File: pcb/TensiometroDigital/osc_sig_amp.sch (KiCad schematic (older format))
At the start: 9 parts

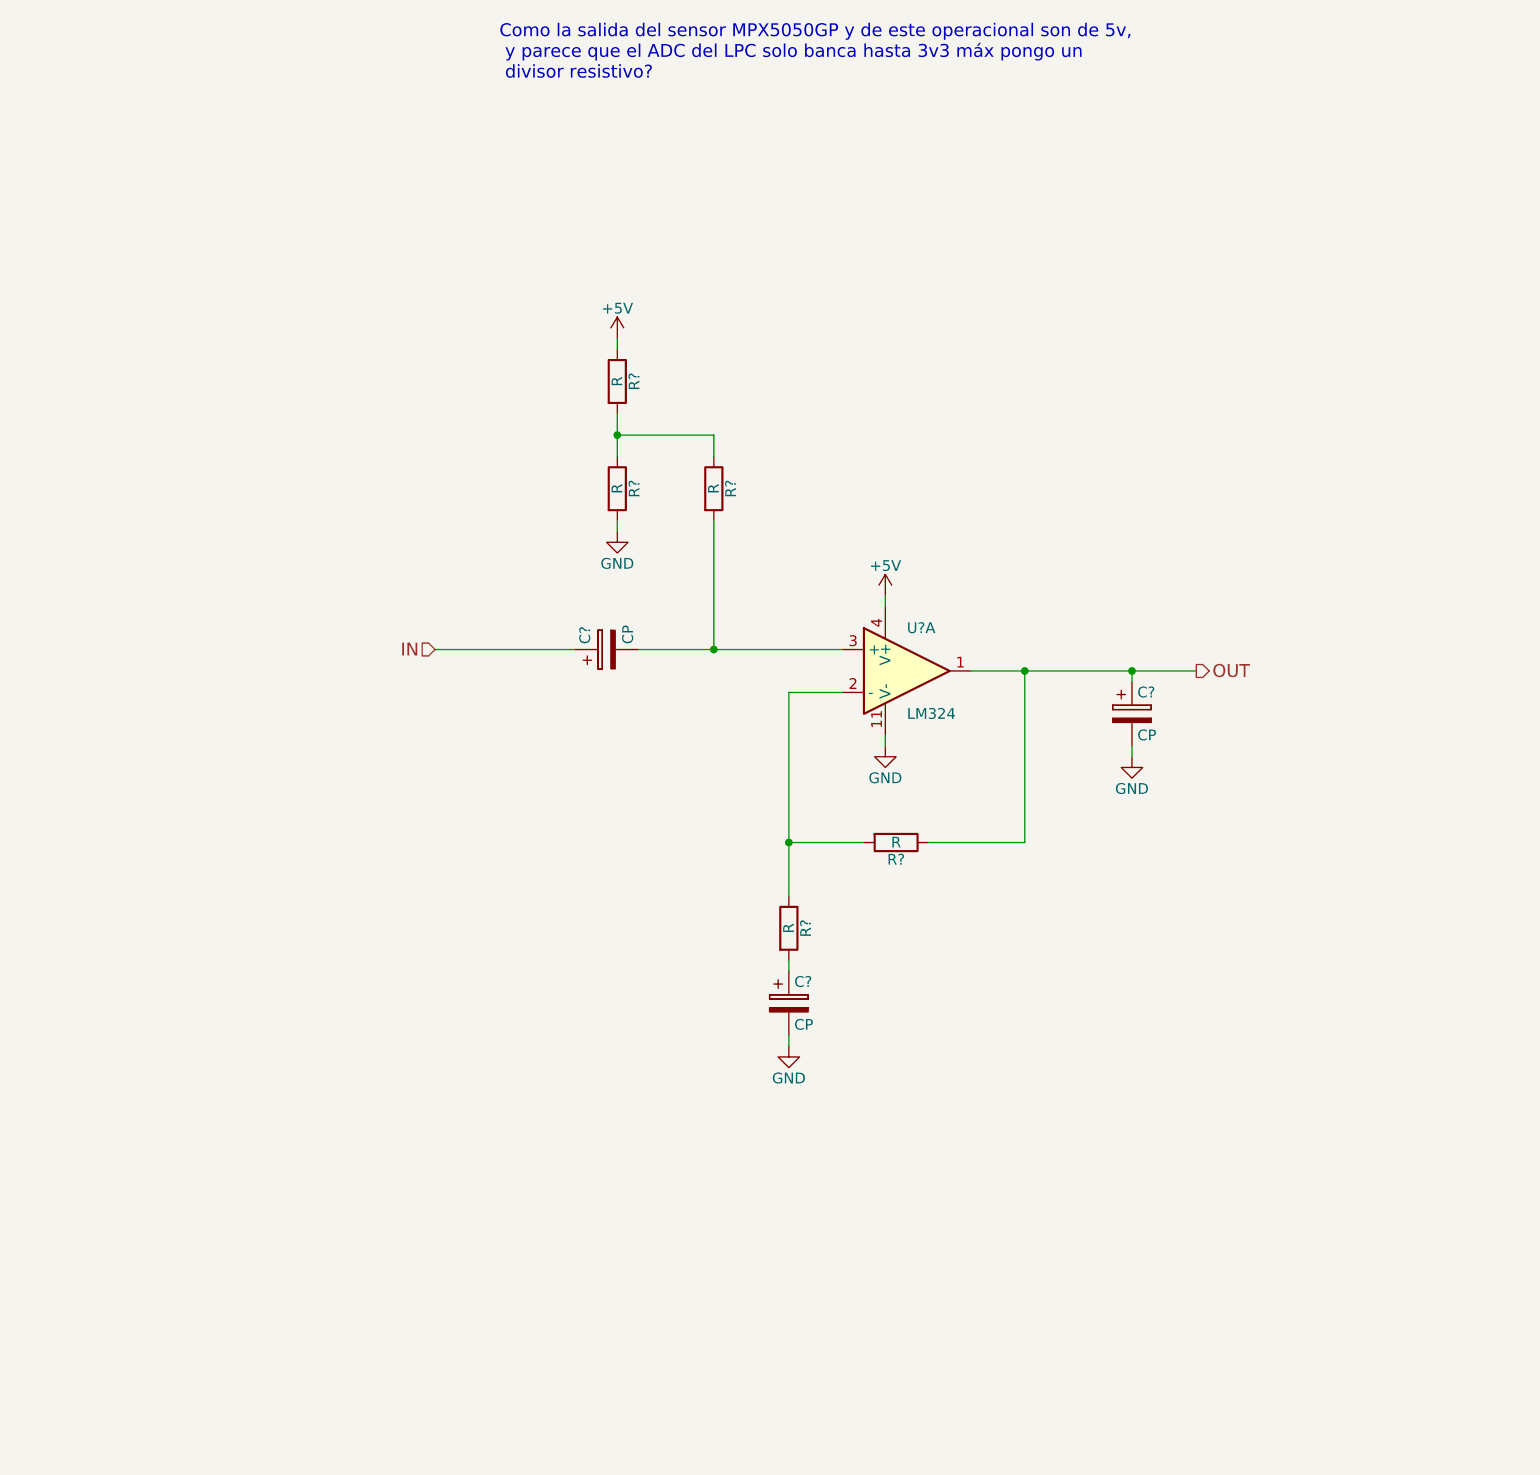
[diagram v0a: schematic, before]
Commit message: Finalizado: SCH, PCB, GABINETE, DRAWINGS. FALTA: GERBERS, BOM e Informe
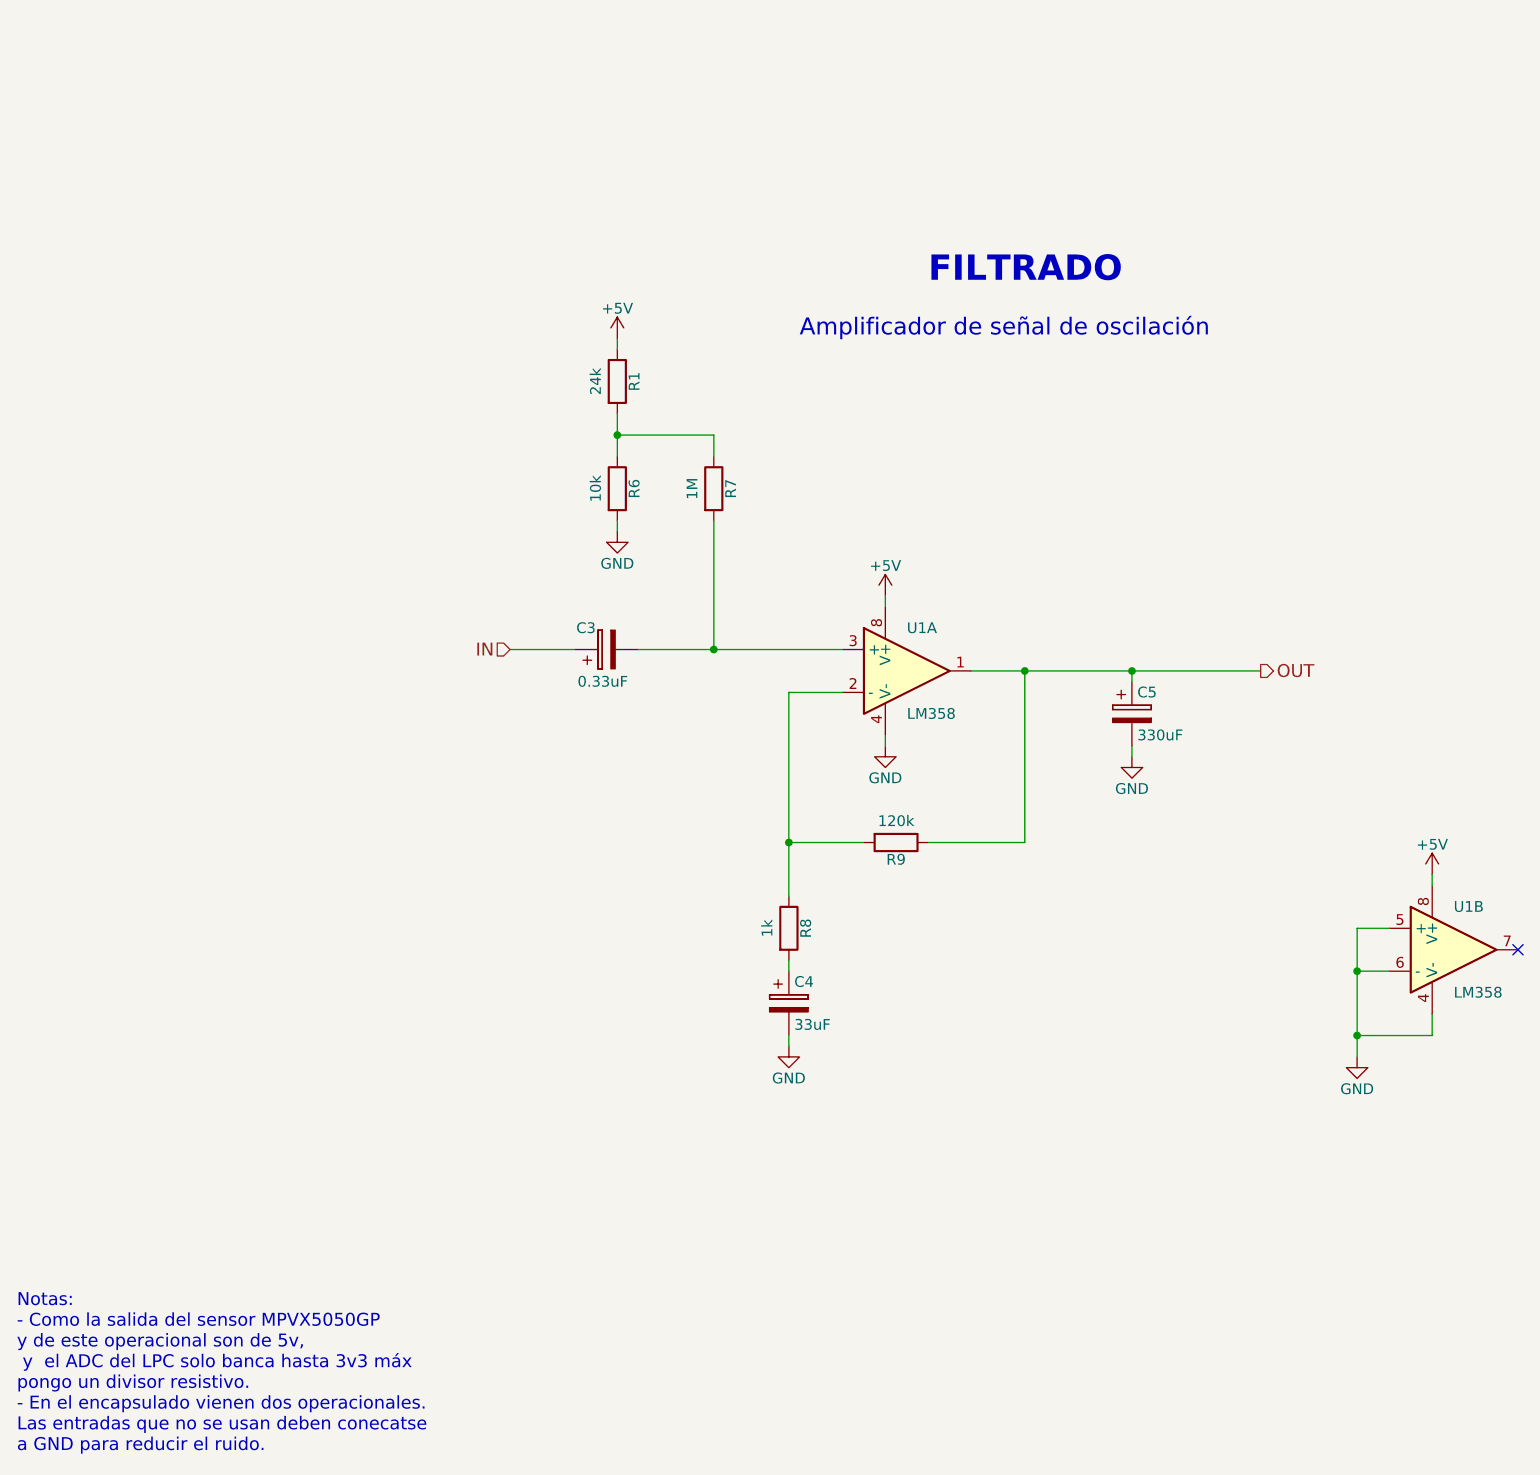
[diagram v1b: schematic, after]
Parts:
- removed U?: LM324, symbol LM324
- added U1: LM358, Housings_SSOP:VSSOP-8_2.3x2mm_Pitch0.5mm, symbol LM358
- C3: renamed from C?; value CP -> 0.33uF; footprint (none) -> Capacitors_SMD:CP_Elec_4x5.7; manf# (none) -> 865230640003
- C4: renamed from C?; value CP -> 33uF; footprint (none) -> Capacitors_SMD:CP_Elec_6.3x4.5; manf# (none) -> UCQ1E330MCL1GB
- C5: renamed from C?; value CP -> 330uF; footprint (none) -> Capacitors_SMD:CP_Elec_8x10.5; manf# (none) -> 865080253011
- R1: renamed from R?; value R -> 24k; footprint (none) -> Resistors_SMD:R_0805_HandSoldering; manf# (none) -> RC0805DR-0724KL
- R6: renamed from R?; value R -> 10k; footprint (none) -> Resistors_SMD:R_0805_HandSoldering; manf# (none) -> SG73G2ATTD1002D
- R7: renamed from R?; value R -> 1M; footprint (none) -> Resistors_SMD:R_0805_HandSoldering; manf# (none) -> SG73G2ATTD1004D
- R8: renamed from R?; value R -> 1k; footprint (none) -> Resistors_SMD:R_0805_HandSoldering; manf# (none) -> SG73G2ATTD1001D
- R9: renamed from R?; value R -> 120k; footprint (none) -> Resistors_SMD:R_0805_HandSoldering; manf# (none) -> RT0805DRE07120KL
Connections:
- net +5V: now also U1.8 (V+), U1.8 (V+)
- net GND: now also U1.4 (V-), U1.4 (V-), U1.5 (+), U1.6 (-)
- net OUT: now also U1.1
- net at R8.1, R9.2: now also U1.2 (-)
- net at C3.2, R7.2: now also U1.3 (+)
- no-connect marks 0 -> 1
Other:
- note added: "Amplificador de señal de oscilación"
- note added: "FILTRADO"
- note added: "Notas:\n- Como la salida del sensor MPVX5050GP \ny de este operacional son de 5v,\n y el ADC del LPC solo banca hasta 3v3 máx \npongo un divisor resistivo.\n- En el encapsulado vienen dos operacionales.\nLas entradas que no se usan deben conecatse\na GND para reducir el ruido."
- note removed: "Como la salida del sensor MPX5050GP y de este operacional son de 5v,\n y parece que el ADC del LPC solo banca hasta 3v3 máx pongo un\n divisor resistivo?"
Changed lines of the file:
@@
 LIBS:lm2940
 LIBS:lm2575
+LIBS:bav199
+LIBS:mpxv5050gp
+LIBS:lm8364
 LIBS:TensiometroDigital-cache
 EELAYER 25 0
@@
 $Descr A4 11693 8268
 encoding utf-8
-Sheet 4 8
-Title ""
-Date ""
-Rev ""
-Comp ""
-Comment1 ""
-Comment2 ""
-Comment3 ""
-Comment4 ""
+Sheet 10 11
+Title "TENSIÓMETRO DIGITAL"
+Date "2018-11-20"
+Rev "A"
+Comp "UTN - FRBA"
+Comment1 "Curso: R1032"
+Comment2 "Leg.: 153204-2"
+Comment3 "Autor: Alegre Mendoza Ezequiel"
+Comment4 "SDR Proyecto Final"
 $EndDescr
 $Comp
-L LM324 U?
-U 1 1 5BBD69A9
-P 5250 3700
-F 0 "U?" H 5250 3900 50  0000 L CNN
-F 1 "LM324" H 5250 3500 50  0000 L CNN
-F 2 "" H 5200 3800 50  0001 C CNN
-F 3 "" H 5300 3900 50  0001 C CNN
-	1    5250 3700
-	1    0    0    -1
-$EndComp
-$Comp
-L R R?
+L R R7
 U 1 1 5BBD6B5D
 P 4350 2850
-F 0 "R?" V 4430 2850 50  0000 C CNN
-F 1 "R" V 4350 2850 50  0000 C CNN
-F 2 "" V 4280 2850 50  0001 C CNN
+F 0 "R7" V 4430 2850 50  0000 C CNN
+F 1 "1M" V 4250 2850 50  0000 C CNN
+F 2 "Resistors_SMD:R_0805_HandSoldering" V 4280 2850 50  0001 C CNN
 F 3 "" H 4350 2850 50  0001 C CNN
+F 4 "SG73G2ATTD1004D" V 4350 2850 60  0001 C CNN "manf#"
 	1    4350 2850
 	1    0    0    -1
 $EndComp
 $Comp
-L R R?
+L R R9
 U 1 1 5BBD6B8E
 P 5200 4500
-F 0 "R?" V 5280 4500 50  0000 C CNN
-F 1 "R" V 5200 4500 50  0000 C CNN
-F 2 "" V 5130 4500 50  0001 C CNN
+F 0 "R9" V 5280 4500 50  0000 C CNN
+F 1 "120k" V 5100 4500 50  0000 C CNN
+F 2 "Resistors_SMD:R_0805_HandSoldering" V 5130 4500 50  0001 C CNN
 F 3 "" H 5200 4500 50  0001 C CNN
+F 4 "RT0805DRE07120KL" V 5200 4500 60  0001 C CNN "manf#"
 	1    5200 4500
 	0    1    1    0
 $EndComp
 $Comp
-L R R?
+L R R8
 U 1 1 5BBD6BAD
 P 4700 4900
-F 0 "R?" V 4780 4900 50  0000 C CNN
-F 1 "R" V 4700 4900 50  0000 C CNN
-F 2 "" V 4630 4900 50  0001 C CNN
+F 0 "R8" V 4780 4900 50  0000 C CNN
+F 1 "1k" V 4600 4900 50  0000 C CNN
+F 2 "Resistors_SMD:R_0805_HandSoldering" V 4630 4900 50  0001 C CNN
 F 3 "" H 4700 4900 50  0001 C CNN
+F 4 "SG73G2ATTD1001D" V 4700 4900 60  0001 C CNN "manf#"
 	1    4700 4900
 	1    0    0    -1
 $EndComp
 $Comp
-L R R?
+L R R1
 U 1 1 5BBD6BD7
 P 3900 2350
-F 0 "R?" V 3980 2350 50  0000 C CNN
-F 1 "R" V 3900 2350 50  0000 C CNN
-F 2 "" V 3830 2350 50  0001 C CNN
+F 0 "R1" V 3980 2350 50  0000 C CNN
+F 1 "24k" V 3800 2350 50  0000 C CNN
+F 2 "Resistors_SMD:R_0805_HandSoldering" V 3830 2350 50  0001 C CNN
 F 3 "" H 3900 2350 50  0001 C CNN
+F 4 "RC0805DR-0724KL" V 3900 2350 60  0001 C CNN "manf#"
 	1    3900 2350
 	1    0    0    -1
 $EndComp
 $Comp
-L R R?
+L R R6
 U 1 1 5BBD6C0A
 P 3900 2850
-F 0 "R?" V 3980 2850 50  0000 C CNN
-F 1 "R" V 3900 2850 50  0000 C CNN
-F 2 "" V 3830 2850 50  0001 C CNN
+F 0 "R6" V 3980 2850 50  0000 C CNN
+F 1 "10k" V 3800 2850 50  0000 C CNN
+F 2 "Resistors_SMD:R_0805_HandSoldering" V 3830 2850 50  0001 C CNN
 F 3 "" H 3900 2850 50  0001 C CNN
+F 4 "SG73G2ATTD1002D " V 3900 2850 60  0001 C CNN "manf#"
 	1    3900 2850
 	1    0    0    -1
 $EndComp
 $Comp
-L CP C?
+L CP C3
 U 1 1 5BBD6C38
 P 3850 3600
-F 0 "C?" H 3875 3700 50  0000 L CNN
-F 1 "CP" H 3875 3500 50  0000 L CNN
-F 2 "" H 3888 3450 50  0001 C CNN
+F 0 "C3" V 3950 3650 50  0000 L CNN
+F 1 "0.33uF" V 3700 3500 50  0000 L CNN
+F 2 "Capacitors_SMD:CP_Elec_4x5.7" H 3888 3450 50  0001 C CNN
 F 3 "" H 3850 3600 50  0001 C CNN
+F 4 "865230640003" V 3850 3600 60  0001 C CNN "manf#"
 	1    3850 3600
 	0    -1   -1   0
 $EndComp
 $Comp
-L CP C?
+L CP C5
 U 1 1 5BBD6C60
 P 6300 3900
-F 0 "C?" H 6325 4000 50  0000 L CNN
-F 1 "CP" H 6325 3800 50  0000 L CNN
-F 2 "" H 6338 3750 50  0001 C CNN
+F 0 "C5" H 6325 4000 50  0000 L CNN
+F 1 "330uF" H 6325 3800 50  0000 L CNN
+F 2 "Capacitors_SMD:CP_Elec_8x10.5" H 6338 3750 50  0001 C CNN
 F 3 "" H 6300 3900 50  0001 C CNN
+F 4 "865080253011" H 6300 3900 60  0001 C CNN "manf#"
 	1    6300 3900
 	1    0    0    -1
 $EndComp
 $Comp
-L CP C?
+L CP C4
 U 1 1 5BBD6C90
 P 4700 5250
-F 0 "C?" H 4725 5350 50  0000 L CNN
-F 1 "CP" H 4725 5150 50  0000 L CNN
-F 2 "" H 4738 5100 50  0001 C CNN
+F 0 "C4" H 4725 5350 50  0000 L CNN
+F 1 "33uF" H 4725 5150 50  0000 L CNN
+F 2 "Capacitors_SMD:CP_Elec_6.3x4.5" H 4738 5100 50  0001 C CNN
 F 3 "" H 4700 5250 50  0001 C CNN
+F 4 "UCQ1E330MCL1GB" H 4700 5250 60  0001 C CNN "manf#"
 	1    4700 5250
 	1    0    0    -1
 $EndComp
 $Comp
-L GND #PWR?
+L GND #PWR062
 U 1 1 5BBD6D8C
 P 3900 3050
-F 0 "#PWR?" H 3900 2800 50  0001 C CNN
+F 0 "#PWR062" H 3900 2800 50  0001 C CNN
 F 1 "GND" H 3900 2900 50  0000 C CNN
 F 2 "" H 3900 3050 50  0001 C CNN
@@
 $EndComp
 $Comp
-L GND #PWR?
+L GND #PWR063
 U 1 1 5BBD6DB9
 P 5150 4050
-F 0 "#PWR?" H 5150 3800 50  0001 C CNN
+F 0 "#PWR063" H 5150 3800 50  0001 C CNN
 F 1 "GND" H 5150 3900 50  0000 C CNN
 F 2 "" H 5150 4050 50  0001 C CNN
@@
 $EndComp
 $Comp
-L GND #PWR?
+L GND #PWR064
 U 1 1 5BBD6DDF
 P 6300 4100
-F 0 "#PWR?" H 6300 3850 50  0001 C CNN
+F 0 "#PWR064" H 6300 3850 50  0001 C CNN
 F 1 "GND" H 6300 3950 50  0000 C CNN
 F 2 "" H 6300 4100 50  0001 C CNN
@@
 $EndComp
 $Comp
-L GND #PWR?
+L GND #PWR065
 U 1 1 5BBD6E05
 P 4700 5450
-F 0 "#PWR?" H 4700 5200 50  0001 C CNN
+F 0 "#PWR065" H 4700 5200 50  0001 C CNN
 F 1 "GND" H 4700 5300 50  0000 C CNN
 F 2 "" H 4700 5450 50  0001 C CNN
@@
 $EndComp
 $Comp
-L +5V #PWR?
+L +5V #PWR066
 U 1 1 5BBD6F0E
 P 5150 3350
-F 0 "#PWR?" H 5150 3200 50  0001 C CNN
+F 0 "#PWR066" H 5150 3200 50  0001 C CNN
 F 1 "+5V" H 5150 3490 50  0000 C CNN
 F 2 "" H 5150 3350 50  0001 C CNN
@@
 $EndComp
 $Comp
-L +5V #PWR?
+L +5V #PWR067
 U 1 1 5BBD6F3B
 P 3900 2150
-F 0 "#PWR?" H 3900 2000 50  0001 C CNN
+F 0 "#PWR067" H 3900 2000 50  0001 C CNN
 F 1 "+5V" H 3900 2290 50  0000 C CNN
 F 2 "" H 3900 2150 50  0001 C CNN
@@
 	1    0    0    -1
 $EndComp
-Text Notes 3350 950  0    60   ~ 0
-Como la salida del sensor MPX5050GP y de este operacional son de 5v,\n y parece que el ADC del LPC solo banca hasta 3v3 máx pongo un\n divisor resistivo?
+Text Notes 1100 7350 0    60   ~ 0
+Notas:\n- Como la salida del sensor MPVX5050GP \ny de este operacional son de 5v,\n y  el ADC del LPC solo banca hasta 3v3 máx \npongo un divisor resistivo.\n- En el encapsulado vienen dos operacionales.\nLas entradas que no se usan deben conecatse\na GND para reducir el ruido.
+Text HLabel 3400 3600 0    60   Input ~ 0
+IN
+Text HLabel 6900 3700 2    60   Output ~ 0
+OUT
 Wire Wire Line
 	4700 5450 4700 5400
@@
 Wire Wire Line
 	5800 4500 5800 3700
-Wire Wire Line
-	5550 3700 6600 3700
 Wire Wire Line
 	6300 3700 6300 3750
@@
 Connection ~ 4700 4500
 Wire Wire Line
-	4950 3600 4000 3600
+	4000 3600 4950 3600
 Wire Wire Line
 	4350 3000 4350 3600
@@
 	5150 4050 5150 4000
 Wire Wire Line
-	3700 3600 3050 3600
-Text HLabel 3050 3600 0    60   Input ~ 0
-IN
-Text HLabel 6600 3700 2    60   Output ~ 0
-OUT
+	3700 3600 3400 3600
+Wire Wire Line
+	5550 3700 6900 3700
+$Comp
+L LM358 U1
+U 1 1 5BDB82A4
+P 5250 3700
+F 0 "U1" H 5250 3900 50  0000 L CNN
+F 1 "LM358" H 5250 3500 50  0000 L CNN
+F 2 "Housings_SSOP:VSSOP-8_2.3x2mm_Pitch0.5mm" H 5250 3700 50  0001 C CNN
+F 3 "" H 5250 3700 50  0001 C CNN
+F 4 "LM358LVIDGKR" H 5250 3700 60  0001 C CNN "manf#"
+	1    5250 3700
+	1    0    0    -1
+$EndComp
+$Comp
+L LM358 U1
+U 2 1 5BDB8348
+P 7800 5000
+F 0 "U1" H 7800 5200 50  0000 L CNN
+F 1 "LM358" H 7800 4800 50  0000 L CNN
+F 2 "Housings_SSOP:VSSOP-8_2.3x2mm_Pitch0.5mm" H 7800 5000 50  0001 C CNN
+F 3 "" H 7800 5000 50  0001 C CNN
+F 4 "LM358LVIDGKR " H 7800 5000 60  0001 C CNN "manf#"
+	2    7800 5000
+	1    0    0    -1
+$EndComp
+$Comp
+L GND #PWR068
+U 1 1 5BDB85ED
+P 7350 5500
+F 0 "#PWR068" H 7350 5250 50  0001 C CNN
+F 1 "GND" H 7350 5350 50  0000 C CNN
+F 2 "" H 7350 5500 50  0001 C CNN
+F 3 "" H 7350 5500 50  0001 C CNN
+	1    7350 5500
+	1    0    0    -1
+$EndComp
+Wire Wire Line
+	7350 4900 7350 5500
+Wire Wire Line
+	7350 4900 7500 4900
+Wire Wire Line
+	7500 5100 7350 5100
+Connection ~ 7350 5100
+Wire Wire Line
+	7700 5300 7700 5400
+Wire Wire Line
+	7700 5400 7350 5400
+Connection ~ 7350 5400
+$Comp
+L +5V #PWR069
+U 1 1 5BDB877F
+P 7700 4650
+F 0 "#PWR069" H 7700 4500 50  0001 C CNN
+F 1 "+5V" H 7700 4790 50  0000 C CNN
+F 2 "" H 7700 4650 50  0001 C CNN
+F 3 "" H 7700 4650 50  0001 C CNN
+	1    7700 4650
+	1    0    0    -1
+$EndComp
+Wire Wire Line
+	7700 4650 7700 4700
+NoConn ~ 8100 5000
+Text Notes 5350 1900 0    118  ~ 24
+FILTRADO
+Text Notes 4750 2150 0    79   ~ 0
+Amplificador de señal de oscilación
 $EndSCHEMATC
